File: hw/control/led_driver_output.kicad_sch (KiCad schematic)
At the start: 9 parts

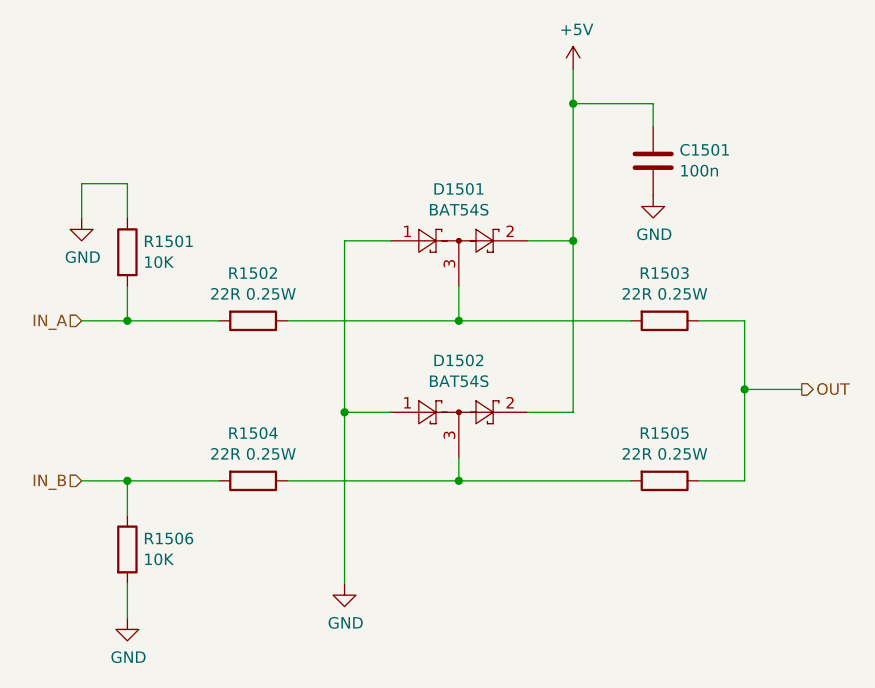
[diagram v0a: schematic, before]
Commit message: [hw] Update to KiCAD 7
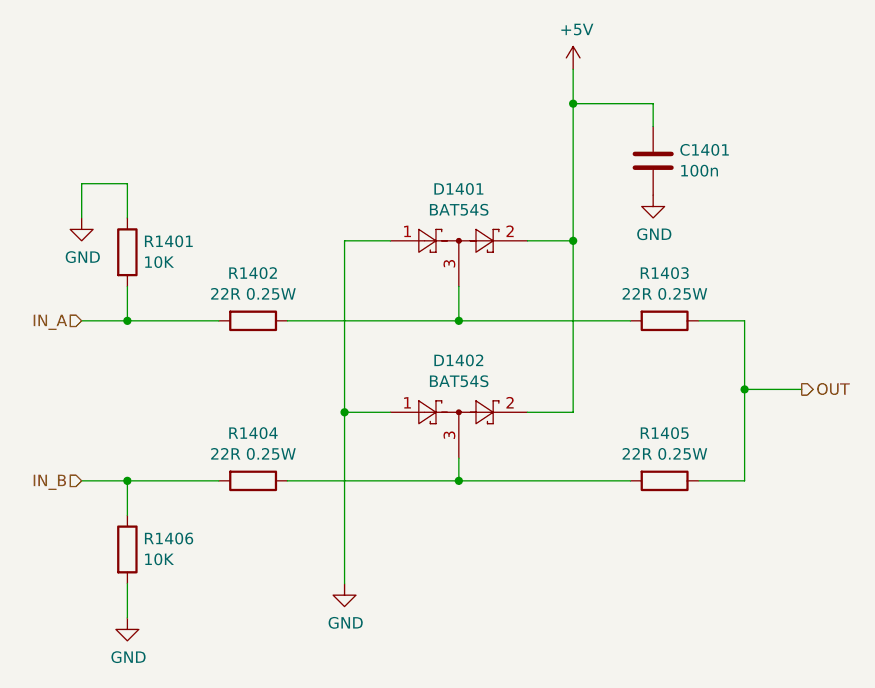
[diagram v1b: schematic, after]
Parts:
- D1401: renamed from D1501; footprint Package_TO_SOT_SMD:SOT-23_Handsoldering -> Package_TO_SOT_SMD:SOT-23
- D1402: renamed from D1502; footprint Package_TO_SOT_SMD:SOT-23_Handsoldering -> Package_TO_SOT_SMD:SOT-23
- renumbered C1501 to C1401, R1501 to R1401, R1502 to R1402, R1503 to R1403, R1504 to R1404, R1505 to R1405, R1506 to R1406
